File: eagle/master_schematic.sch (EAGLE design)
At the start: 92 parts, among them U1 TPS73633DBVR

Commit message: Cleanup
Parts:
- removed C13, C19, C20, C21, C22, C23: (no value), resistor:C-EUC1206
- removed JP3, JP4: (no value), pinhead:PINHD-1X2
- removed JP5: (no value), pinhead:PINHD-2X3
- removed LED11, LED12, LED13, LED14, LED15, LED16, LED17, LED18: SFH482, led:SFH482
- removed PWR_LED: green, led:LED3MM
- removed R4, R5: 6 ohm, resistor:R-US_R1206
- removed R6: 10 ohm, resistor:R-US_R1206
- added BAT_1, BAT_2: (no value), SparkFun-Connectors:JST_2MM_MALE
- added C1_F_EMITS, C1_L_EMIT, C1_R_EMIT: 4.7uF, resistor:C-EUC1206
- added C2_F_EMITS, C2_L_EMIT: .1uF, resistor:C-EUC1206
- added C2_R_EMIT: .1 uF, resistor:C-EUC1206
- added LED1, LED2, LED3, LED4, LED5, LED6, LED7, LED8, LED9: (no value), led:LEDCHIPLED_0603
- added LF_IR_EMIT, L_IR_EMIT, RF_IR_EMIT, R_IR_EMIT: 5mm, led:LED5MM
- added PROG_HEAD: (no value), pinhead:PINHD-2X4
- added R_LEFT, R_RIGHT: 6 ohm, resistor:R-US_R1206
- added R_LF: 10 ohm, resistor:R-US_R1206
- C1_LMOT, C1_RMOT: value 100nF -> 100uF
- C2_LMOT, C2_RMOT: value 100nF -> .1uF
- LED10: value SFH482 -> PWR_LED; device led:SFH482 -> led:LEDCHIPLED_0805
- R1_LMOT, R1_RMOT, R2_LMOT, R2_RMOT: value (none) -> 47k
- R_PWR: device resistor:R-US_M1206 -> resistor:R-US_M0805
- U2: value TPS76850 -> TPS76850QD
- renumbered C1 to C1_BAT, C10 to C_5, C11 to C_3, C12 to C_4, C14 to C1_LMOT, C15 to C1_3.3V, C16 to C2_3.3V, C17 to C3_3.3V, C18 to C2_LMOT, C2 to C1_A, C3 to VCAP2, C4 to VCAP1, C5 to C2_A, C6 to C1_RMOT, C7 to C2_RMOT, C8 to C_1, C9 to C_2, C_5V_3 to C1_5V, C_5V_4 to C2_5V, C_RESET2 to C_US_1, JP1 to R_MOT, JP2 to L_MOT, L3 to L_5.0V, L4 to L_3.3V, R1 to R1_RMOT, R12 to R1_LMOT, R13 to R2_LMOT, R18 to R_LED9, R19 to R_LED8, R2 to R2_RMOT, R20 to R_LED7, R21 to R_LED6, R22 to R_LED5, R23 to R_LED4, R24 to R_LED3, R25 to R_LED2, R26 to R_LED1, R3 to R_RF, SW1 to PWR_SWTCH, U$2 to U2
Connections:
- removed net N$29: R6.2
- removed net PE: C13.2, C19.2, C1_LMOT.1, C1_RMOT.1, C20.2, C21.2, C22.2, C23.2, C2_LMOT.1, C2_RMOT.1, C_L_L1.2, C_L_R1.2, R_LF_R1.1, R_L_R1.1, R_RF_R1.1, R_R_R1.1, U$10.GND, U$11.N1S/N2S, U$13.GND, U$14.N1S/N2S, U$4.E
- removed net VDD: JP5.1
- new net C_US_2: C_RESET3.1, R_SW2.1, S2.S
- new net N$26: L_IR_EMIT.C, R_LEFT.2
- new net N$33: PROG_HEAD.8
- new net N$34: PROG_HEAD.6
- new net N$9: BAT_1.-, BAT_2.+
- net 3.3V: now also PROG_HEAD.1
- net 5V: now also C1_F_EMITS.2, C1_L_EMIT.2, C1_R_EMIT.2, C2_F_EMITS.2, C2_L_EMIT.2, C2_R_EMIT.2, LF_IR_EMIT.A, L_IR_EMIT.A, RF_IR_EMIT.A, R_IR_EMIT.A; no longer C13.1, C19.1, C20.1, C21.1, C22.1, C23.1, L_MOT.3, R_MOT.3
- net A5.0V: now also L_MOT.3, R_MOT.3
- net GND: now also BAT_2.-, C1_F_EMITS.1, C1_L_EMIT.1, C1_R_EMIT.1, C2_F_EMITS.1, C2_L_EMIT.1, C2_R_EMIT.1, C_L_L1.2, C_L_R1.2, LED1.C, LED2.C, LED3.C, LED4.C, LED5.C, LED6.C, LED7.C, LED8.C, LED9.C, PROG_HEAD.3, R_LF_R1.1, R_L_R1.1, R_RF_R1.1, R_R_R1.1, U$4.E; no longer JP4.2, JP5.2, LED11.C, LED12.C, LED13.C, LED14.C, LED15.C, LED16.C, LED17.C, LED18.C, PWR_LED.C
- net GND1: now also C1_LMOT.1, C1_RMOT.1, C2_LMOT.1, C2_RMOT.1, U$10.GND, U$11.N1S/N2S, U$13.GND, U$14.N1S/N2S
- net N$1: now also LED10.A; no longer PWR_LED.A
- net N$15: now also U$1.PB5; no longer JP3.2, JP4.1
- net N$23: now also RF_IR_EMIT.C
- net N$24: now also R_RIGHT.1; no longer R4.1
- net N$25: now also R_IR_EMIT.C, R_RIGHT.2; no longer R4.2
- net N$27: now also R_LEFT.1; no longer R5.1
- net N$28: now also LF_IR_EMIT.C, R_LF.2; no longer R5.2
- net N$30: now also R_LF.1; no longer R6.1
- net N$31: now also BAT_1.+, PWR_SWTCH.2; no longer JP3.1
- net N$40: now also LED1.A; no longer LED18.A
- net N$41: now also LED2.A; no longer LED17.A
- net N$42: now also LED3.A; no longer LED16.A
- net N$43: now also LED4.A; no longer LED15.A
- net N$44: now also LED5.A; no longer LED14.A
- net N$45: now also LED6.A; no longer LED13.A
- net N$46: now also LED7.A; no longer LED12.A
- net N$47: now also LED8.A; no longer LED11.A
- net N$48: now also LED9.A; no longer LED10.A
- net N$7: now also U$1.PB6; no longer U$4.1C
- net RX: now also PROG_HEAD.5; no longer JP5.4
- net SWCLK: now also PROG_HEAD.4; no longer JP5.6
- net SWDIO: now also PROG_HEAD.2; no longer JP5.5
- net TX: now also PROG_HEAD.7; no longer JP5.3
- net US_2: no longer C_RESET3.1, R_SW2.1, S2.S
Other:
- note added: "Pinout: Pin 1: Pin 2: Pin 3: Pin 4: Pin 5: Pin 6:"
- note added: "Right Motor"
- note added: "VBAT"
- note added: "VDDA/VSSA"
- note removed: "ULN2003APWR"

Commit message: Updated Schematic + Gyroscope
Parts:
- removed U$11, U$14: H-BRIDGE, MMHbridge:H-BRIDGE
- removed VCAP1: 2.2uF, rcl:C-USC0603
- added C1: 100nF, rcl:C-USC0603
- added C2, C4, C5: 1uF, rcl:C-USC0603
- added C_VCAP1: 2.2uF, rcl:C-USC0603
- added D1: >24V, diode:DIODE-SOD123
- added G1: ADXRS810, gyroscope:ADXRS810
- added HB_L, HB_R: ZXMHC3F381N8TC, MMHbridge:ZXMHC3F381N8TC
- added L1: 470uH, resistor:L-USL1812
- BAT_1, BAT_2: value (none) -> JST_2mm
- BOOT0: value (none) -> A_HIGH
- LED1, LED2, LED3, LED4, LED5, LED6, LED7, LED8, LED9: value (none) -> 0805
- PROG_HEAD: value (none) -> 2x4
- RST, S2, S3: value (none) -> A_LOW
- renumbered U$10 to MOS_L, U$13 to MOS_R, U1 to 33LDO, U2 to 50LDO, VCAP2 to C_VCAP2
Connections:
- removed net LPWMA: MOS_L.IN_A, R1_LMOT.2, U$1.PA3, U$1.PD12
- removed net N$14: U$1.PA1
- removed net TDS-SWO: U$1.PB3
- new net GYRO_CS: G1.CS
- new net G_MISO: G1.MISO
- new net G_MOSI: G1.MOSI
- new net G_SCLK: G1.SCLK
- new net LPWM: MOS_L.IN_A, R1_LMOT.2, U$1.PA1
- new net N$35: C2.1, G1.AV_DD
- net A3.3V: now also C4.1, G1.PDD, L1.1
- net GND: now also C1.2, C2.2, C4.2, C5.2, C_VCAP1.2, G1.AV_SS, G1.DV_SS, G1.PSS, G1.RSVD@1, G1.RSVD@2, G1.RSVD@3, G1.RSVD@4; no longer VCAP1.2
- net GND1: now also HB_L.N1S/N2S, HB_R.N1S/N2S; no longer U$11.N1S/N2S, U$14.N1S/N2S
- net LED1: now also U$1.PD4; no longer U$1.PD6
- net LPWMB: no longer U$1.PD13
- net N$10: now also C5.1, G1.DV_DD; no longer U$11.P1G
- net N$11: now also HB_L.N2D/P2D; no longer U$11.N2D/P2D
- net N$17: now also HB_R.N1G; no longer U$14.N1G
- net N$18: now also HB_R.N2G, HB_R.P2G; no longer U$14.N2G, U$14.P2G
- net N$19: now also HB_R.N1D/P1D; no longer U$14.N1D/P1D
- net N$20: now also C1.1, G1.CP5, G1.V_X, L1.2; no longer U$14.P1G
- net N$21: now also HB_R.N2D/P2D; no longer U$14.N2D/P2D
- net N$4: now also C_VCAP1.1; no longer VCAP1.1
- net N$5: now also HB_L.N1G; no longer U$11.N1G
- net N$6: now also HB_L.N2G, HB_L.P2G; no longer U$11.N2G, U$11.P2G
- net N$8: now also HB_L.N1D/P1D; no longer U$11.N1D/P1D
- net RPWMA: no longer U$1.PA0-WKUP, U$1.PD14
- net RPWMB: no longer U$1.PD15
- net V_BAT: now also HB_L.P1S/P2S, HB_R.P1S/P2S; no longer U$11.P1S/P2S, U$14.P1S/P2S
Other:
- note removed: "Pins 59 - 62 are TIM4 pins"

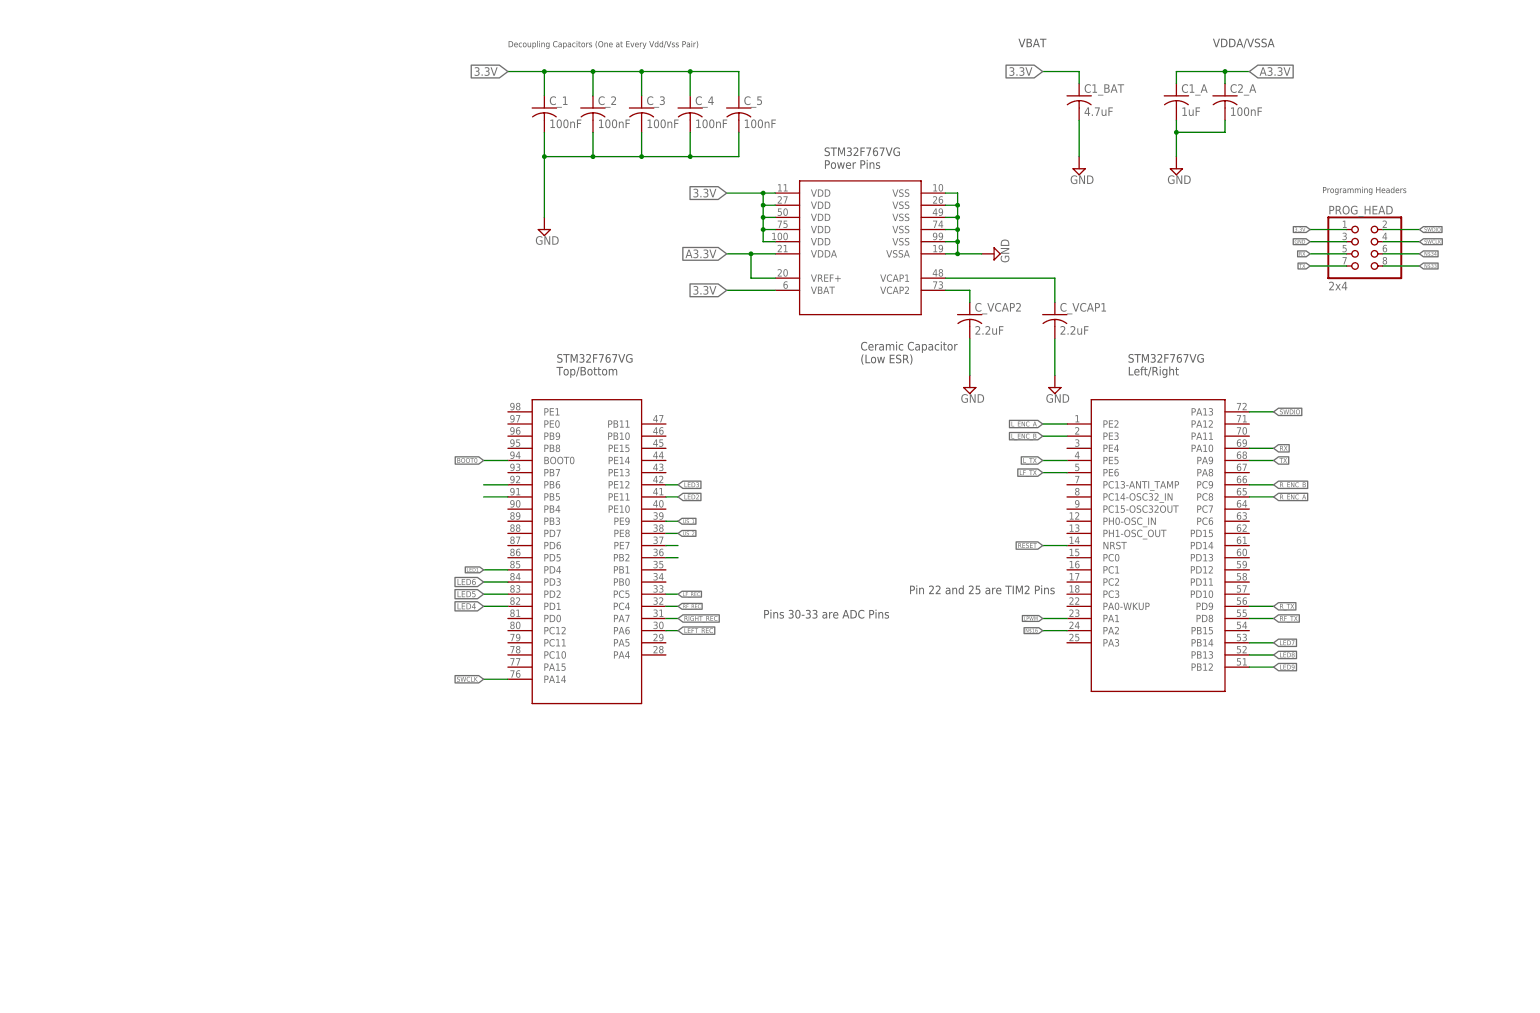
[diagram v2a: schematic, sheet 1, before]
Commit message: Added Buzzer
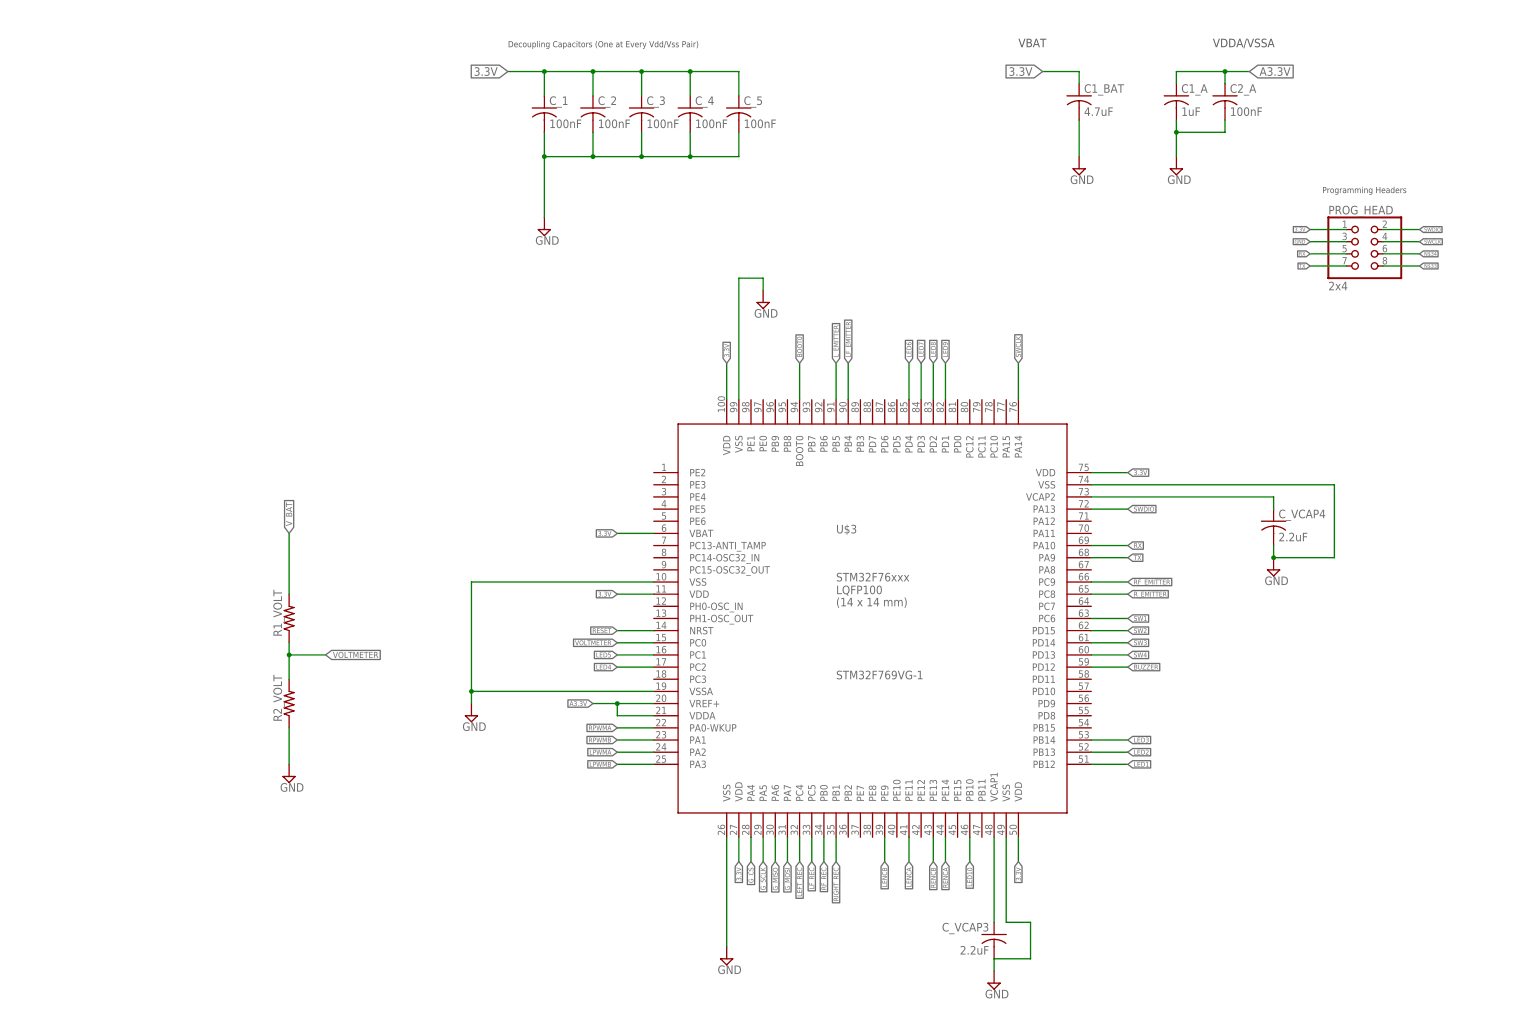
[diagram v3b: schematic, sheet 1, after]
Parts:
- removed C_VCAP1, C_VCAP2: 2.2uF, rcl:C-USC0603
- removed PWR_SWTCH: (no value), special:SW_DIP-1
- removed U$1: STM32F767VG(2), MCU:STM32F767VG(2)
- added C_VCAP3, C_VCAP4: 2.2uF, rcl:C-USC0603
- added D2: 25V, diode:DIODE-SOD123
- added PWR_SWITCH: T212031, GCswitch:T212031
- added R1_VOLT, R2_VOLT: (no value), resistor:R-US_R0805
- added SPK1: SMT-0540-S-R, SMT-0540-S-R:SMT-0540-S-R
- added U$3: STM32F769VG-1, MCU:STM32F769VG-1
- L_MOT: value (none) -> L1
- R_MOT: value (none) -> R1
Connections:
- removed net C_US_2: C_RESET3.1, R_SW2.1, S2.S
- removed net GYRO_CS: G1.CS
- removed net LF_TX: U$1.PE6
- removed net LPWM: MOS_L.IN_A, R1_LMOT.2, U$1.PA1
- removed net L_ENC_A: L_MOT.1, U$1.PE2
- removed net L_ENC_B: L_MOT.2, U$1.PE3
- removed net L_TX: U$1.PE5
- removed net N$12: U$1.PE7
- removed net N$13: U$1.PB2
- removed net N$15: U$1.PB5
- removed net N$16: U$1.PA2
- removed net N$3: C_VCAP2.1, U$1.VCAP2
- removed net N$4: C_VCAP1.1, U$1.VCAP1
- removed net N$7: U$1.PB6
- removed net RF_TX: U$1.PD8
- removed net R_ENC_A: R_MOT.1, U$1.PC8
- removed net R_ENC_B: R_MOT.2, U$1.PC9
- removed net R_TX: U$1.PD9
- removed net US_1: C_US_1.1, R_SW1.1, S3.S, U$1.PE9
- removed net US_2: U$1.PE8
- new net BUZZER: U$3.PD12, U$4.1B
- new net G_CS: G1.CS, U$3.PA4
- new net LED10: U$3.PB10
- new net LENCA: L_MOT.1, U$3.PE11
- new net LENCB: L_MOT.2, U$3.PE9
- new net LPWMA: MOS_L.IN_A, R1_LMOT.2, U$3.PA2
- new net N$14: D1.A, G1.V_X, L1.2
- new net N$29: D2.A, SPK1.-, U$4.1C
- new net N$56: C_VCAP4.1, U$3.VCAP2
- new net N$57: C_VCAP3.1, U$3.VCAP1
- new net RENCA: R_MOT.1, U$3.PE14
- new net RENCB: R_MOT.2, U$3.PE13
- new net SW1: C_US_1.1, R_SW1.1, S3.S, U$3.PC6
- new net SW2: C_RESET3.1, R_SW2.1, S2.S, U$3.PD15
- new net SW3: U$3.PD14
- new net SW4: U$3.PD13
- new net VOLTMETER: R1_VOLT.1, R2_VOLT.2, U$3.PC0
- net 3.3V: now also D2.C, SPK1.+, U$3.VBAT, U$3.VDD@1, U$3.VDD@2, U$3.VDD@3, U$3.VDD@4, U$3.VDD@5; no longer U$1.VBAT, U$1.VDD@1, U$1.VDD@2, U$1.VDD@3, U$1.VDD@4, U$1.VDD@5
- net A3.3V: now also U$3.VDDA, U$3.VREF+; no longer U$1.VDDA, U$1.VREF+
- net BOOT0: now also U$3.BOOT0; no longer U$1.BOOT0
- net GND: now also C_VCAP3.2, C_VCAP4.2, R2_VOLT.1, U$3.VSS@1, U$3.VSS@2, U$3.VSS@3, U$3.VSS@4, U$3.VSS@5, U$3.VSSA; no longer C_VCAP1.2, C_VCAP2.2, U$1.VSS@1, U$1.VSS@2, U$1.VSS@3, U$1.VSS@4, U$1.VSS@5, U$1.VSSA
- net G_MISO: now also U$3.PA6
- net G_MOSI: now also U$3.PA7
- net G_SCLK: now also U$3.PA5
- net LED1: now also U$3.PB12; no longer U$1.PD4
- net LED2: now also U$3.PB13; no longer U$1.PE11
- net LED3: now also U$3.PB14; no longer U$1.PE12
- net LED4: now also U$3.PC2; no longer U$1.PD1
- net LED5: now also U$3.PC1; no longer U$1.PD2
- net LED6: now also U$3.PD4; no longer U$1.PD3
- net LED7: now also U$3.PD3; no longer U$1.PB14
- net LED8: now also U$3.PD2; no longer U$1.PB13
- net LED9: now also U$3.PD1; no longer U$1.PB12
- net LEFT_REC: now also U$3.PC4; no longer U$1.PA6
- net LF_EMITTER: now also U$3.PB4
- net LF_REC: now also U$3.PC5; no longer U$1.PC5
- net LPWMB: now also U$3.PA3
- net L_EMITTER: now also U$3.PB5
- net N$20: now also D1.C; no longer G1.V_X, L1.2
- net N$31: now also PWR_SWITCH.2; no longer PWR_SWTCH.2
- net RESET: now also U$3.NRST; no longer U$1.NRST
- net RF_EMITTER: now also U$3.PC9
- net RF_REC: now also U$3.PB0; no longer U$1.PC4
- net RIGHT_REC: now also U$3.PB1; no longer U$1.PA7
- net RPWMA: now also U$3.PA0-WKUP
- net RPWMB: now also U$3.PA1
- net RX: now also U$3.PA10; no longer U$1.PA10
- net R_EMITTER: now also U$3.PC8
- net SWCLK: now also U$3.PA14; no longer U$1.PA14
- net SWDIO: now also U$3.PA13; no longer U$1.PA13
- net TX: now also U$3.PA9; no longer U$1.PA9
- net V_BAT: now also PWR_SWITCH.3, R1_VOLT.2; no longer PWR_SWTCH.1
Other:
- note added: "Pinout: Pin 1: LENCA- IN Pin 2: LENCB - IN Pin 3: 5.0V - OUT Pin 4: GND Pin 5: M1 - OUT Pin 6: M2 - OUT"
- note added: "Pinout: Pin 1: RENCA- IN Pin 2: RENCB - IN Pin 3: 5.0V - OUT Pin 4: GND Pin 5: M1 - OUT Pin 6: M2 - OUT"
- note added: "switch"
- note removed: "Ceramic Capacitor (Low ESR)"
- note removed: "On/Off Switch"
- note removed: "Pin 22 and 25 are TIM2 Pins"
- note removed: "Pinout: Pin 1: Pin 2: Pin 3: Pin 4: Pin 5: Pin 6:"
- note removed: "Pins 30-33 are ADC Pins"
- moved on the sheet: C5
